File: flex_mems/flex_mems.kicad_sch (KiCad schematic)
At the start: 20 parts, among them J1 10164227-0101A1RLF, J2 10164227-0101A1RLF

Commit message: Schematics done
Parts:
- added C7, C8: 2.2uF, Capacitor_SMD:C_0402_1005Metric, symbol Device:C_Small
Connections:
- net +3V3L: now also C7.1
- net +3V3R: now also C8.1
- net GNDL: now also C7.2
- net GNDR: now also C8.2

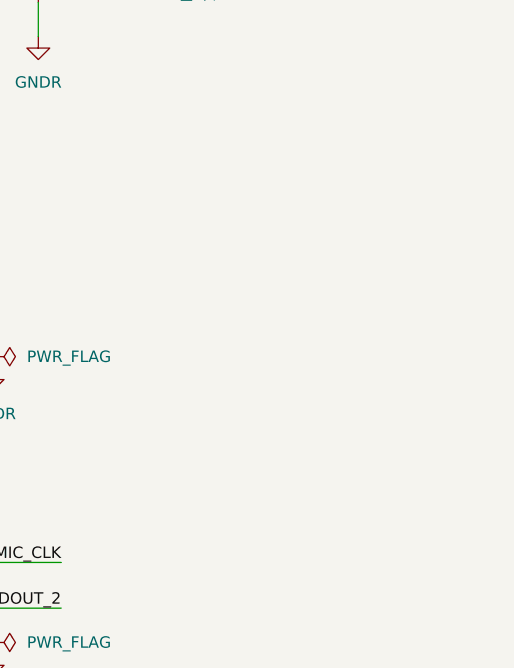
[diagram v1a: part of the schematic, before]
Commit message: GND zone update
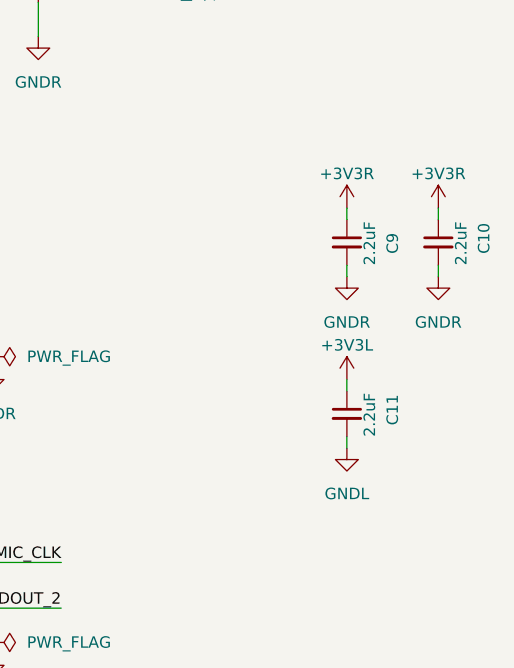
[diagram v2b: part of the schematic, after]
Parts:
- added C10, C11, C9: 2.2uF, Capacitor_SMD:C_0402_1005Metric, symbol Device:C_Small
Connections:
- net +3V3L: now also C11.1
- net +3V3R: now also C10.1, C9.1
- net GNDL: now also C11.2
- net GNDR: now also C10.2, C9.2
